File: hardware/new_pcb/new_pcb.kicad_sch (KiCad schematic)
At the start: 15 parts, among them J1 01x16_LCD, K1 01x16_Keypad, Q1 IRLZ34N, U1 ESP32-DevKitC

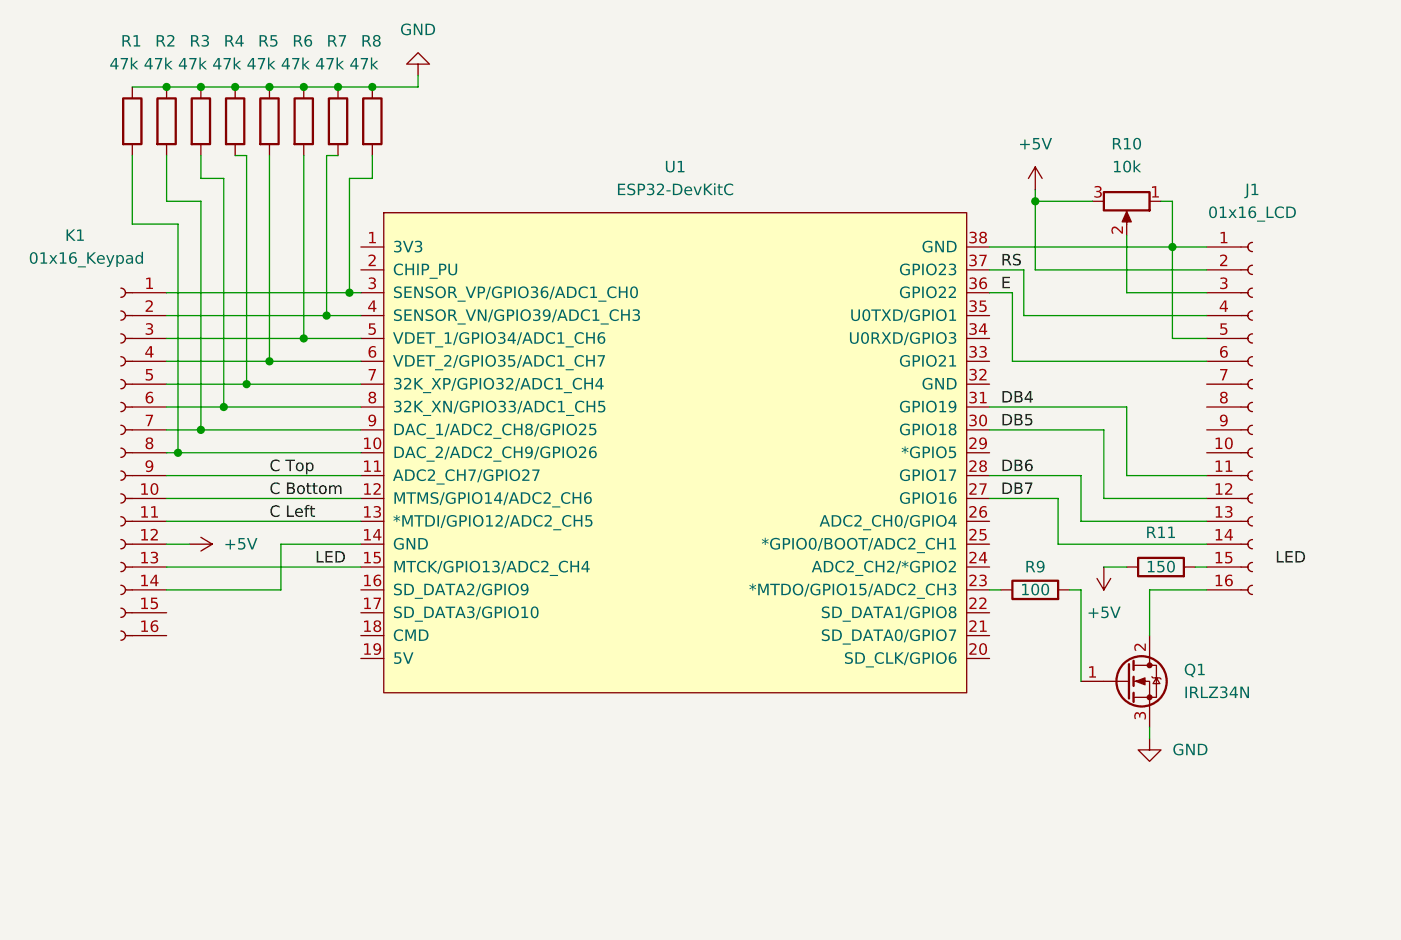
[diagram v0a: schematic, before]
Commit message: Add DS18B20 temperature sensor
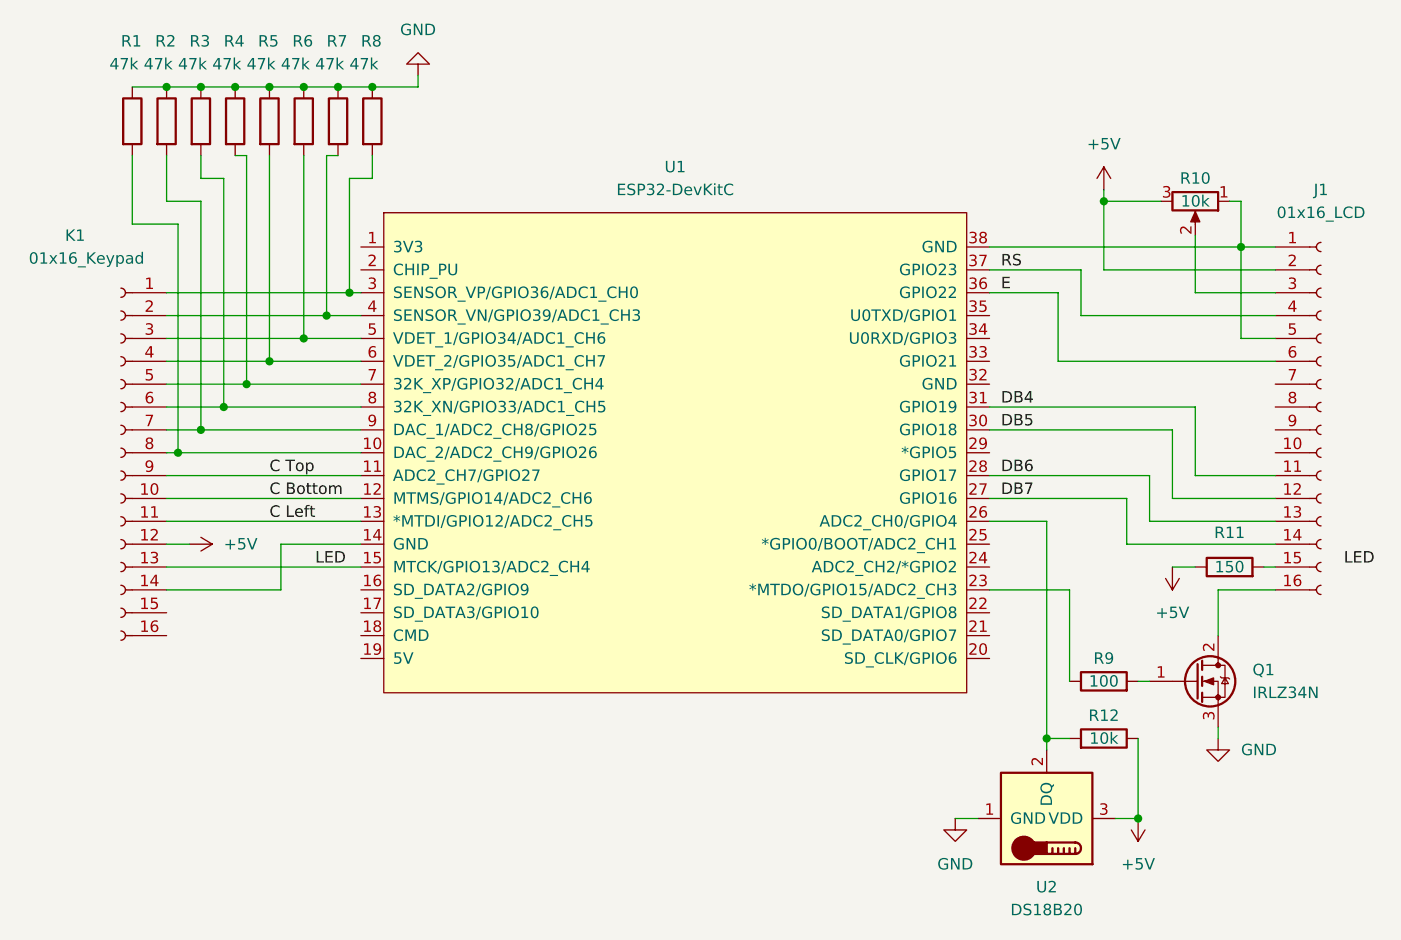
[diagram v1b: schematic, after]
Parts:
- added R12: 10k, symbol Device:R
- added U2: DS18B20, Package_TO_SOT_THT:TO-92_Inline, symbol Sensor_Temperature:DS18B20
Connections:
- net +5V: now also R12.1, U2.3 (VDD)
- net GND: now also U2.1 (GND)
- net at U1.26 (ADC2_CH0/GPIO4): now also R12.2, U2.2 (DQ)
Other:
- moved on the sheet: J1, Q1, R10, R11, R9

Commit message: Add new pcb schematics description
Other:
- company: (none) -> Zdenek Veleba
- title: (none) -> BS 100 New controller
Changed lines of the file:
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@@
 (kicad_sch (version 20211123) (generator eeschema)
   (paper "A4")
+  (title_block
+    (title "BS 100 New controller")
+    (date "2023-04-10")
+    (rev "2.00")
+    (company "Zdenek Veleba")
+  )
   (junction (at 109.22 78.74) (diameter 0) (color 0 0 0 0)
   )
